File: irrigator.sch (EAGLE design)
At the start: 27 parts, among them IC1 MEGA8-AI, IC2 78L05Z, T1 BT136, X1 MSTBA2

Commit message: fix. errors and manual routing
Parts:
- C3: device rcl:C-EU102-054X133 -> rcl:C-EUC1206
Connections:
- new net MISO: IC1.PB4(MISO), JP3.1
- new net MOSI: IC1.PB3(MOSI/OC2), JP3.4
- new net SCK: IC1.PB5(SCK), JP3.3
- net BUTTON_1: now also IC1.PB1(OC1A); no longer IC1.PB0(ICP)
- net BUTTON_2: now also IC1.PB0(ICP); no longer IC1.PB1(OC1A)
- net LED_1: now also IC1.PD5(T1); no longer IC1.PB3(MOSI/OC2), JP3.4
- net LED_2: now also IC1.PD6(AIN0); no longer IC1.PB4(MISO), JP3.1
- net SENS_IN: no longer JP3.3
- net SW: now also IC1.PD3(INT1); no longer IC1.PB2(SS/OC1B)
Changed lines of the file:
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@@
 <?xml version="1.0" encoding="utf-8"?>
 <!DOCTYPE eagle SYSTEM "eagle.dtd">
-<eagle version="7.6.0">
+<eagle version="7.7.0">
 <drawing>
 <settings>
@@
 <part name="R7" library="resistor" deviceset="R-EU_" device="R1206" value="180"/>
 <part name="R8" library="resistor" deviceset="R-EU_" device="R1206" value="2.4k"/>
-<part name="C3" library="rcl" deviceset="C-EU" device="102-054X133" value="100n"/>
+<part name="C3" library="rcl" deviceset="C-EU" device="C1206" value="100n"/>
 <part name="R9" library="resistor" deviceset="R-EU_" device="R1206" value="300"/>
 <part name="GND13" library="supply1" deviceset="GND" device=""/>
@@
 </segment>
 <segment>
-<pinref part="IC1" gate="G$1" pin="PB1(OC1A)"/>
-<wire x1="142.24" y1="40.64" x2="144.78" y2="40.64" width="0.1524" layer="91"/>
-<label x="147.32" y="40.64" size="1.778" layer="95"/>
+<pinref part="IC1" gate="G$1" pin="PB0(ICP)"/>
+<wire x1="142.24" y1="43.18" x2="144.78" y2="43.18" width="0.1524" layer="91"/>
+<label x="147.32" y="43.18" size="1.778" layer="95"/>
 </segment>
 </net>
@@
 </segment>
 <segment>
-<pinref part="IC1" gate="G$1" pin="PB0(ICP)"/>
-<wire x1="142.24" y1="43.18" x2="144.78" y2="43.18" width="0.1524" layer="91"/>
-<label x="147.32" y="43.18" size="1.778" layer="95"/>
+<pinref part="IC1" gate="G$1" pin="PB1(OC1A)"/>
+<wire x1="142.24" y1="40.64" x2="144.78" y2="40.64" width="0.1524" layer="91"/>
+<label x="147.32" y="40.64" size="1.778" layer="95"/>
 </segment>
 </net>
@@
 <pinref part="JP3" gate="A" pin="5"/>
 <wire x1="152.4" y1="15.24" x2="144.78" y2="15.24" width="0.1524" layer="91"/>
-<label x="139.7" y="2.54" size="1.778" layer="95"/>
+<label x="139.7" y="12.7" size="1.778" layer="95"/>
 </segment>
 <segment>
@@
 </segment>
 <segment>
-<pinref part="JP3" gate="A" pin="4"/>
-<wire x1="160.02" y1="17.78" x2="167.64" y2="17.78" width="0.1524" layer="91"/>
-</segment>
-<segment>
-<pinref part="IC1" gate="G$1" pin="PB3(MOSI/OC2)"/>
-<wire x1="142.24" y1="35.56" x2="144.78" y2="35.56" width="0.1524" layer="91"/>
-<label x="147.32" y="35.56" size="1.778" layer="95"/>
+<pinref part="IC1" gate="G$1" pin="PD5(T1)"/>
+<wire x1="142.24" y1="53.34" x2="147.32" y2="53.34" width="0.1524" layer="91"/>
+<label x="147.32" y="53.34" size="1.778" layer="95"/>
 </segment>
 </net>
@@
 </segment>
 <segment>
-<pinref part="JP3" gate="A" pin="1"/>
-<wire x1="152.4" y1="20.32" x2="144.78" y2="20.32" width="0.1524" layer="91"/>
-</segment>
-<segment>
-<pinref part="IC1" gate="G$1" pin="PB4(MISO)"/>
-<wire x1="142.24" y1="33.02" x2="144.78" y2="33.02" width="0.1524" layer="91"/>
-<label x="147.32" y="33.02" size="1.778" layer="95"/>
+<pinref part="IC1" gate="G$1" pin="PD6(AIN0)"/>
+<wire x1="142.24" y1="50.8" x2="147.32" y2="50.8" width="0.1524" layer="91"/>
+<label x="147.32" y="50.8" size="1.778" layer="95"/>
 </segment>
 </net>
@@
 </segment>
 <segment>
-<pinref part="JP3" gate="A" pin="3"/>
-<wire x1="152.4" y1="17.78" x2="144.78" y2="17.78" width="0.1524" layer="91"/>
-</segment>
-<segment>
 <pinref part="IC1" gate="G$1" pin="PC0(ADC0)"/>
 <wire x1="142.24" y1="88.9" x2="144.78" y2="88.9" width="0.1524" layer="91"/>
@@
 </segment>
 <segment>
-<pinref part="IC1" gate="G$1" pin="PB2(SS/OC1B)"/>
-<wire x1="142.24" y1="38.1" x2="144.78" y2="38.1" width="0.1524" layer="91"/>
-<label x="147.32" y="38.1" size="1.778" layer="95"/>
+<pinref part="IC1" gate="G$1" pin="PD3(INT1)"/>
+<wire x1="142.24" y1="58.42" x2="147.32" y2="58.42" width="0.1524" layer="91"/>
+<label x="147.32" y="58.42" size="1.778" layer="95"/>
 </segment>
 </net>
@@
 </segment>
 </net>
+<net name="SCK" class="0">
+<segment>
+<pinref part="IC1" gate="G$1" pin="PB5(SCK)"/>
+<wire x1="142.24" y1="30.48" x2="144.78" y2="30.48" width="0.1524" layer="91"/>
+<label x="147.32" y="30.48" size="1.778" layer="95"/>
+</segment>
+<segment>
+<pinref part="JP3" gate="A" pin="3"/>
+<wire x1="152.4" y1="17.78" x2="144.78" y2="17.78" width="0.1524" layer="91"/>
+<label x="139.7" y="17.78" size="1.778" layer="95"/>
+</segment>
+</net>
+<net name="MISO" class="0">
+<segment>
+<pinref part="IC1" gate="G$1" pin="PB4(MISO)"/>
+<wire x1="142.24" y1="33.02" x2="144.78" y2="33.02" width="0.1524" layer="91"/>
+<label x="147.32" y="33.02" size="1.778" layer="95"/>
+</segment>
+<segment>
+<pinref part="JP3" gate="A" pin="1"/>
+<wire x1="152.4" y1="20.32" x2="144.78" y2="20.32" width="0.1524" layer="91"/>
+<label x="139.7" y="20.32" size="1.778" layer="95"/>
+</segment>
+</net>
+<net name="MOSI" class="0">
+<segment>
+<pinref part="IC1" gate="G$1" pin="PB3(MOSI/OC2)"/>
+<wire x1="142.24" y1="35.56" x2="144.78" y2="35.56" width="0.1524" layer="91"/>
+<label x="147.32" y="35.56" size="1.778" layer="95"/>
+</segment>
+<segment>
+<pinref part="JP3" gate="A" pin="4"/>
+<wire x1="160.02" y1="17.78" x2="167.64" y2="17.78" width="0.1524" layer="91"/>
+<label x="165.1" y="17.78" size="1.778" layer="95"/>
+</segment>
+</net>

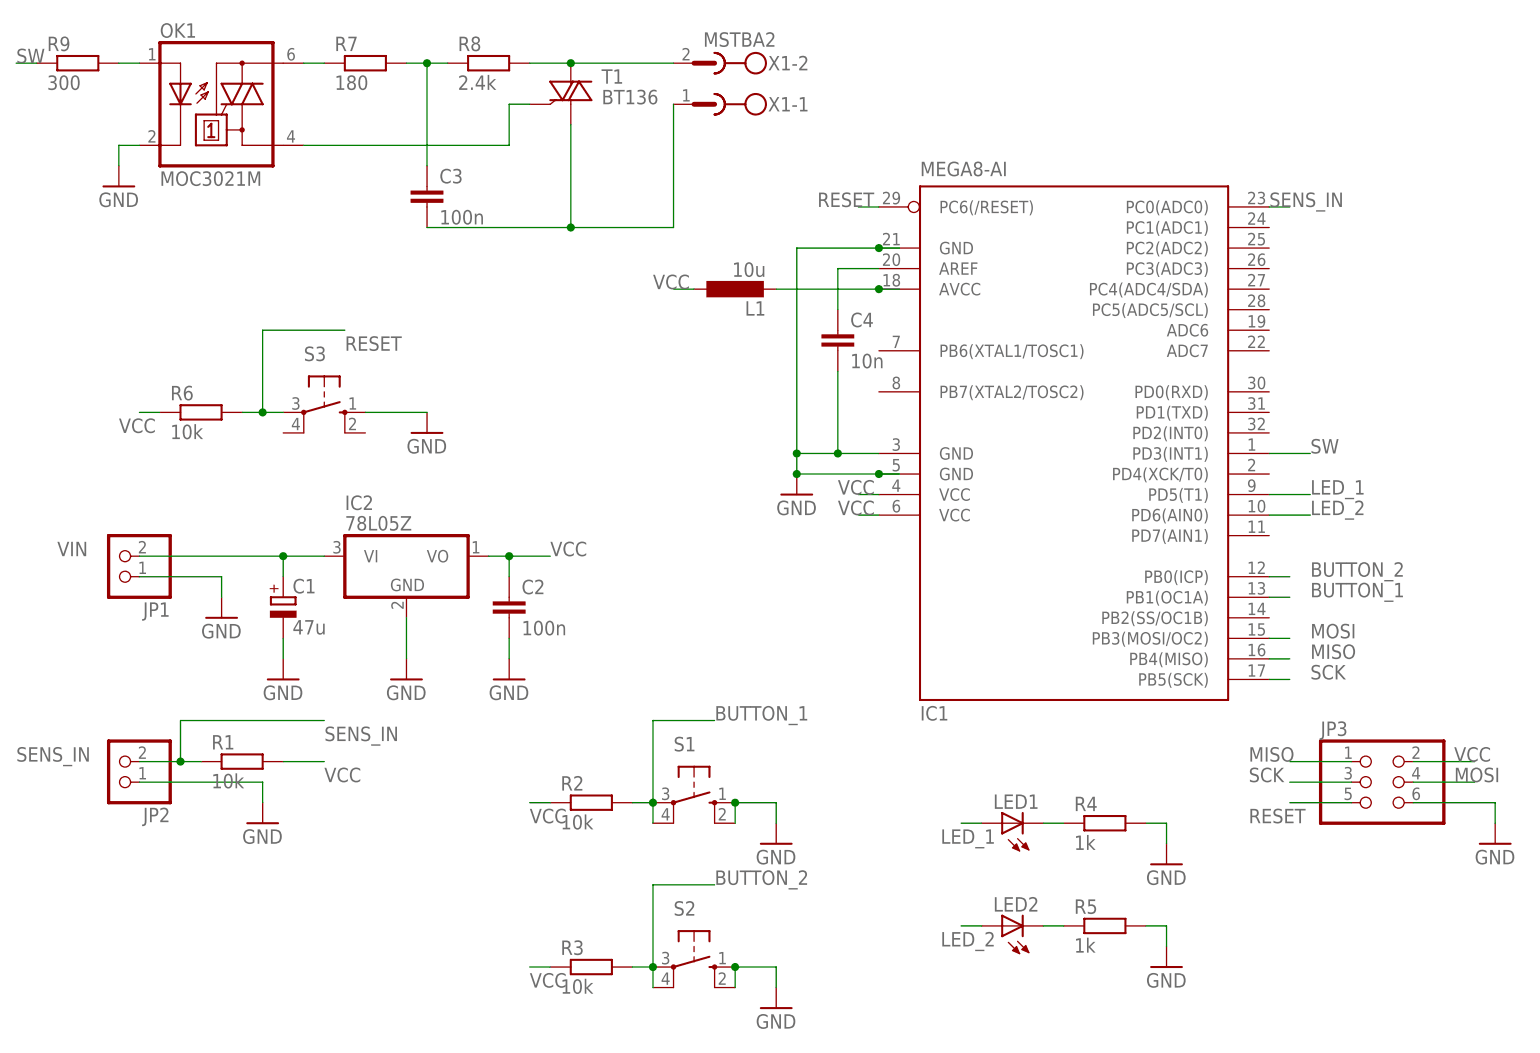
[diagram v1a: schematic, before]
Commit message: add sensor switch
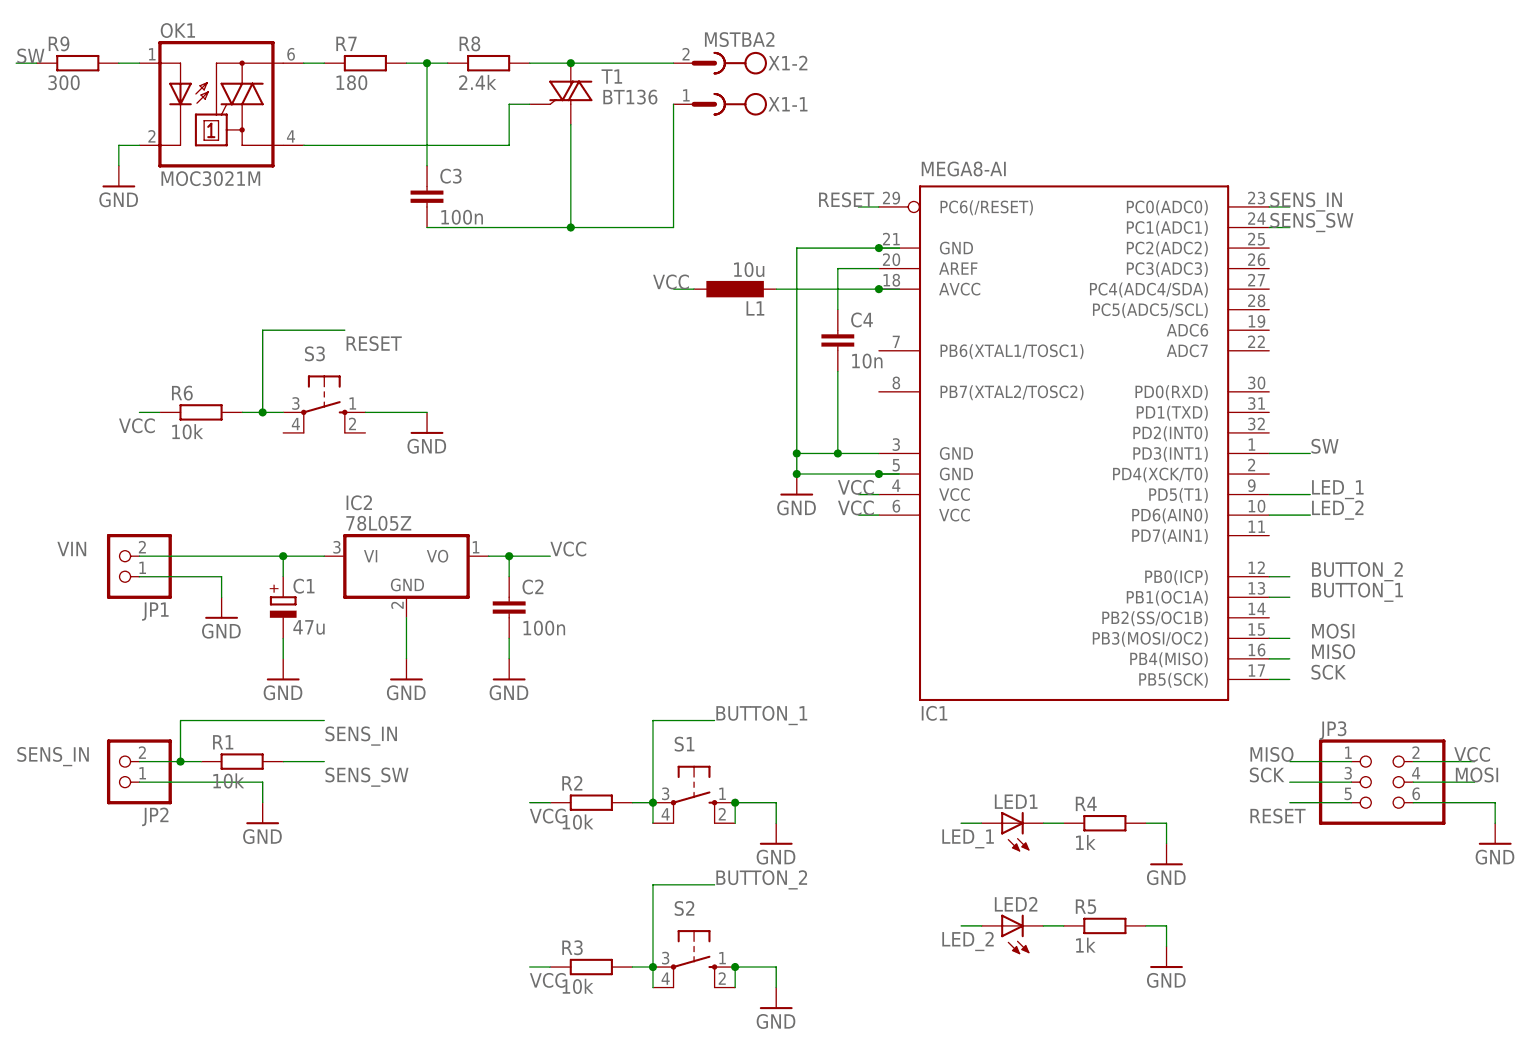
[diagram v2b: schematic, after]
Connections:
- new net SENS_SW: IC1.PC1(ADC1), R1.2
- net VCC: no longer R1.2
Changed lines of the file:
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@@
 <?xml version="1.0" encoding="utf-8"?>
 <!DOCTYPE eagle SYSTEM "eagle.dtd">
-<eagle version="7.7.0">
+<eagle version="8.0.0">
 <drawing>
 <settings>
@@
 </segment>
 <segment>
-<pinref part="R1" gate="G$1" pin="2"/>
-<wire x1="20.32" y1="20.32" x2="25.4" y2="20.32" width="0.1524" layer="91"/>
-<label x="25.4" y="17.78" size="1.778" layer="95"/>
-</segment>
-<segment>
 <pinref part="R2" gate="G$1" pin="1"/>
 <wire x1="53.34" y1="15.24" x2="50.8" y2="15.24" width="0.1524" layer="91"/>
@@
 </segment>
 </net>
+<net name="SENS_SW" class="0">
+<segment>
+<pinref part="R1" gate="G$1" pin="2"/>
+<wire x1="20.32" y1="20.32" x2="25.4" y2="20.32" width="0.1524" layer="91"/>
+<label x="25.4" y="17.78" size="1.778" layer="95"/>
+</segment>
+<segment>
+<pinref part="IC1" gate="G$1" pin="PC1(ADC1)"/>
+<wire x1="142.24" y1="86.36" x2="144.78" y2="86.36" width="0.1524" layer="91"/>
+<label x="142.24" y="86.36" size="1.778" layer="95"/>
+</segment>
+</net>
